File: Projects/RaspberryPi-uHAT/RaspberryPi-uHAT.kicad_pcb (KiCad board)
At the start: 2 copper layers, 65 x 30 mm, 5 parts, among them J1 GPIO

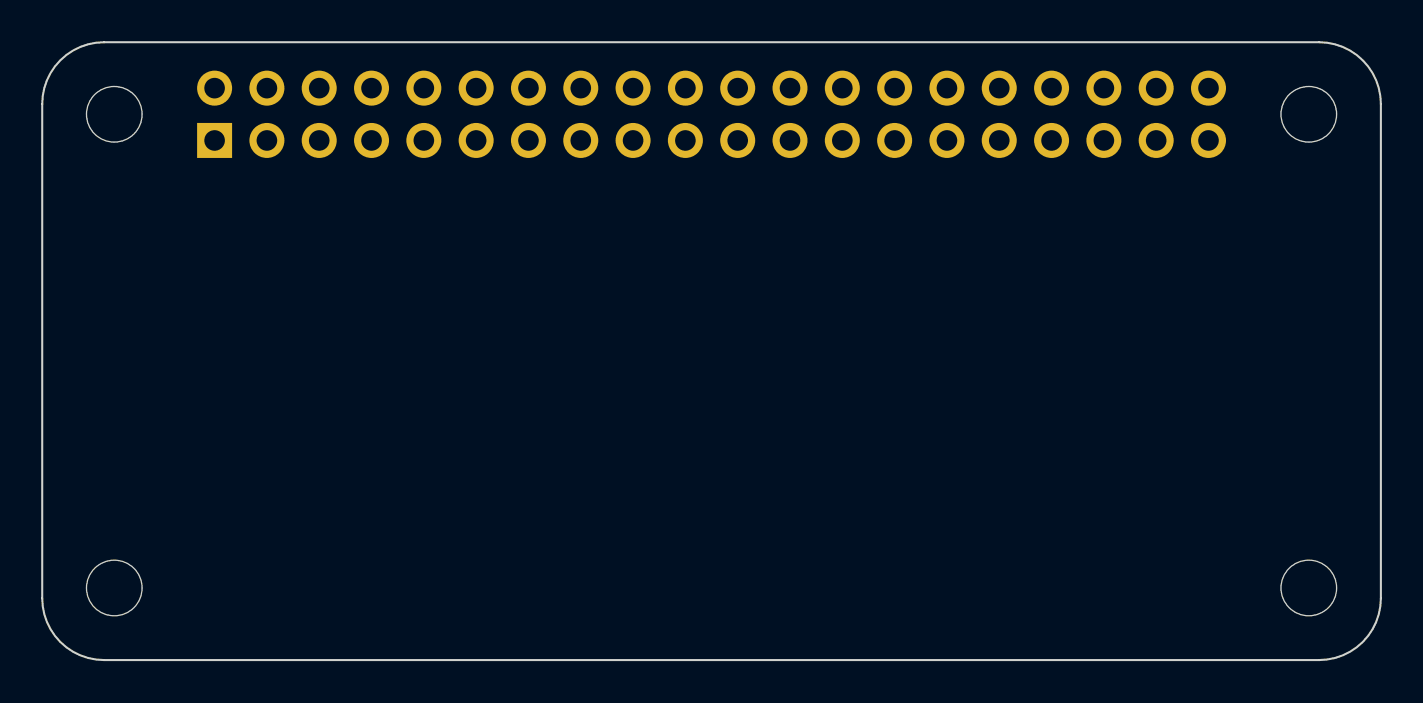
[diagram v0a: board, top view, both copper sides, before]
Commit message: adding parts placer to raspberrypi-uhat
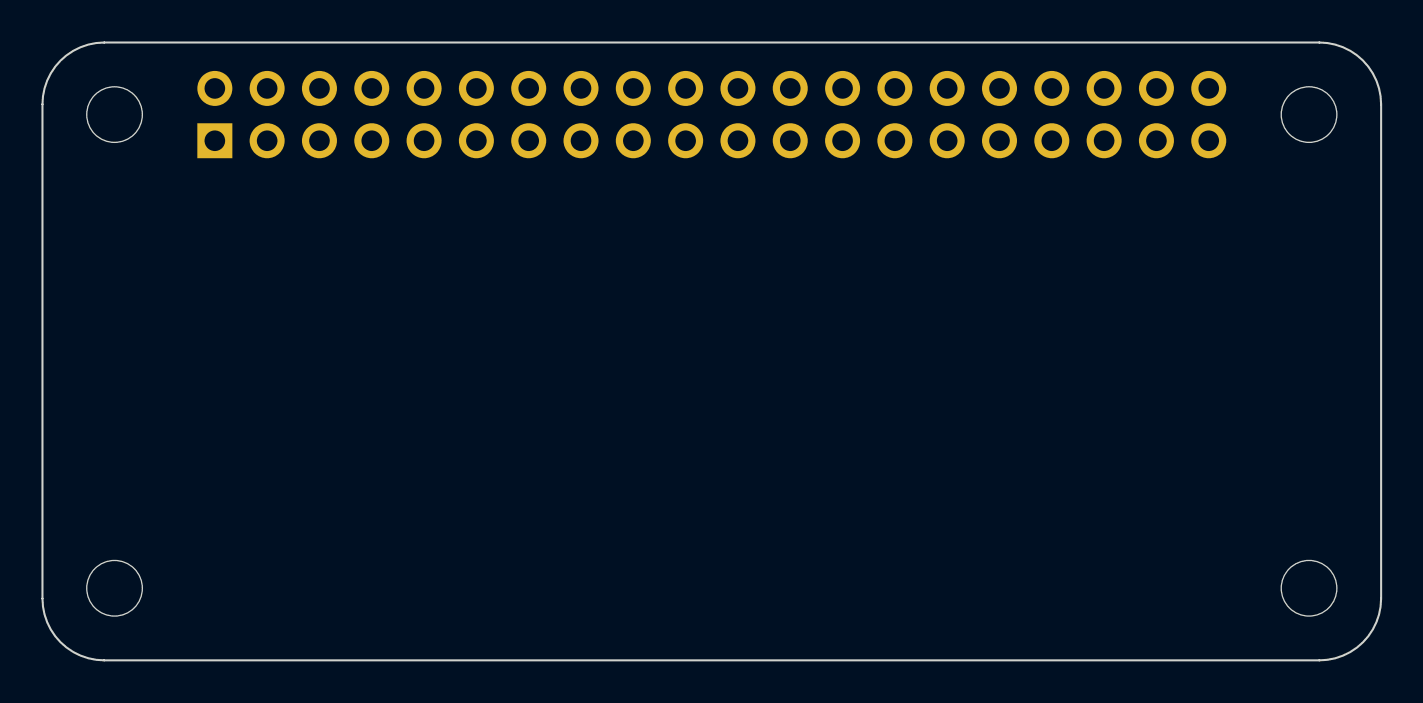
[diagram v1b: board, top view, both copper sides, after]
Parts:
- added BOARD: board, Library:board, F.Cu at (132.5, 85.0)
- moved MH1 62.4 mm to (161.5, 96.5)
- moved MH4 62.4 mm to (103.5, 73.5)
